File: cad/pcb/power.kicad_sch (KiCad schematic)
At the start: 32 parts, among them X1 USB_C_Plug, X2 Bat-Conn

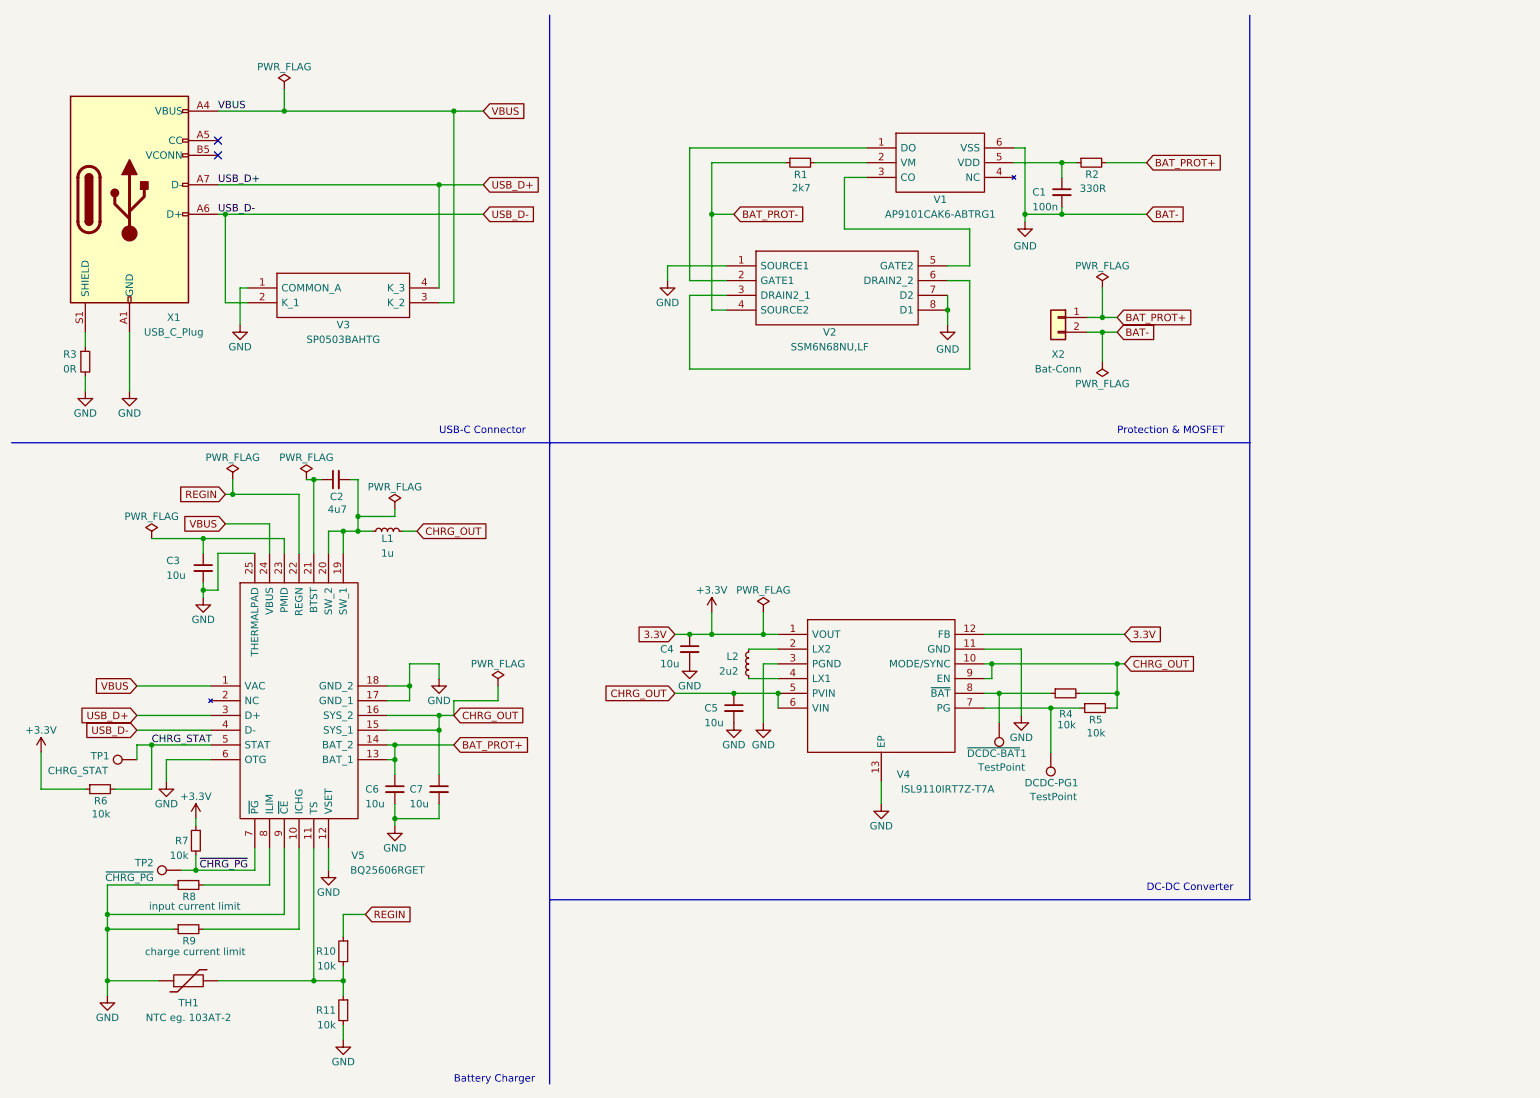
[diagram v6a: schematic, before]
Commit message: add testpoints & connectors
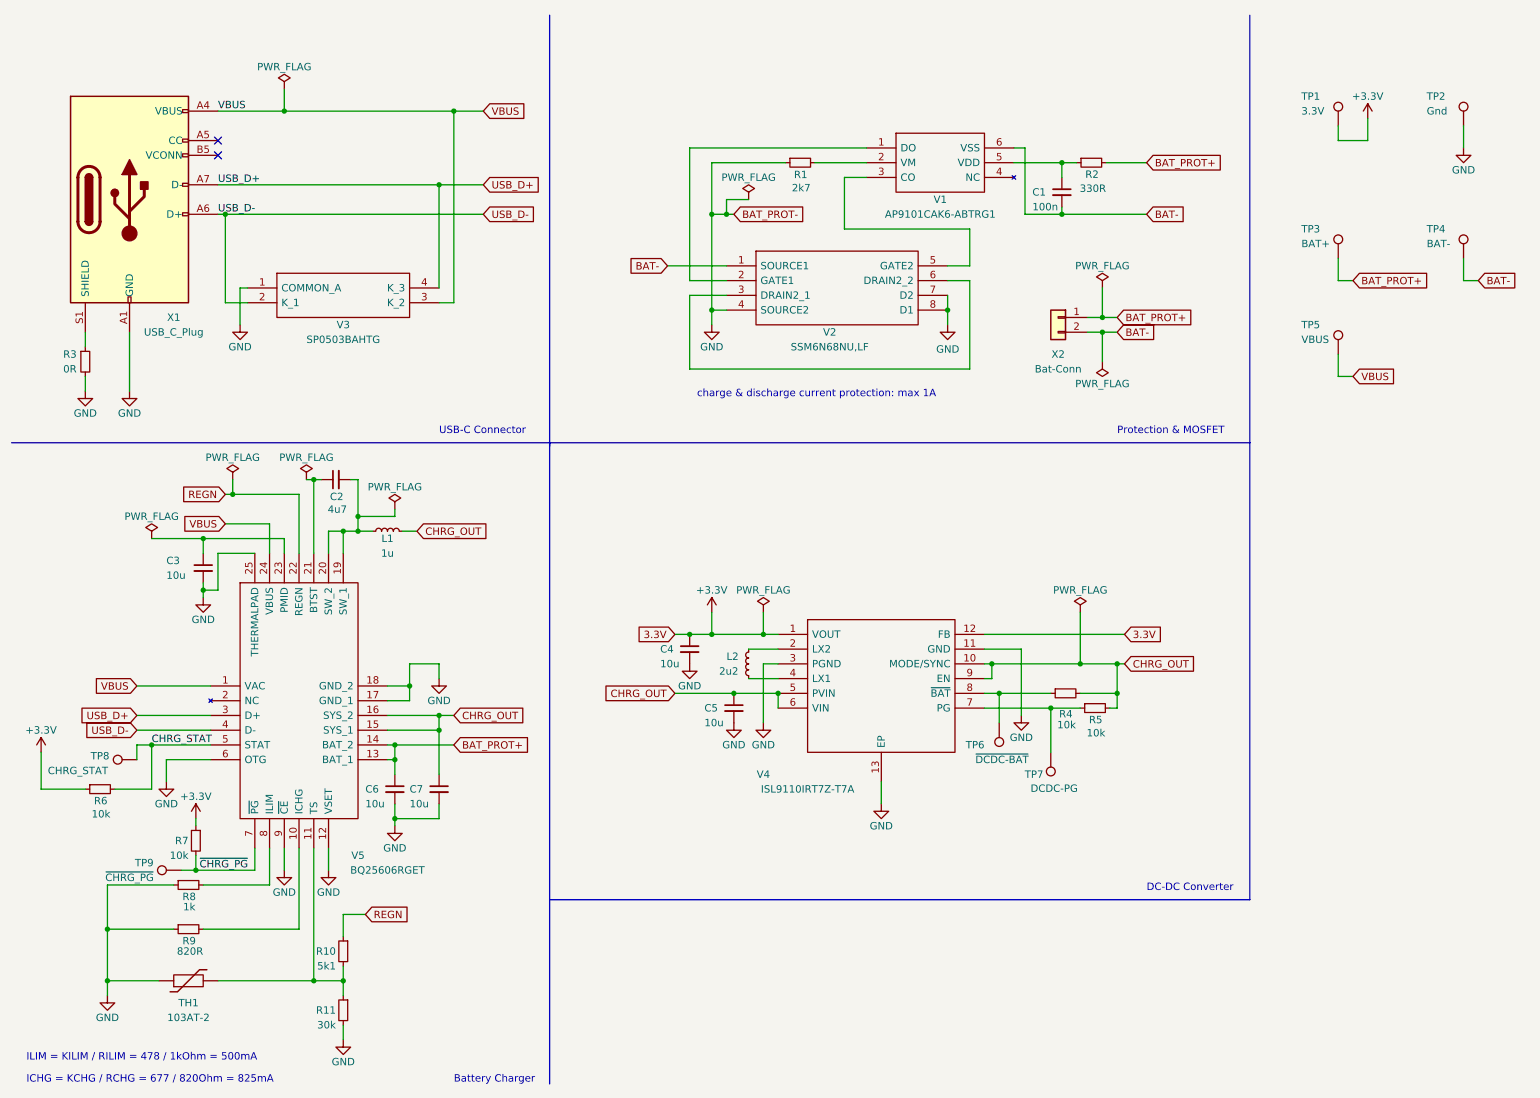
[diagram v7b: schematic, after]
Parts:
- added TP1: 3.3V, symbol Connector:TestPoint
- added TP2: Gnd, symbol Connector:TestPoint
- added TP3: BAT+, symbol Connector:TestPoint
- added TP4: BAT-, symbol Connector:TestPoint
- added TP5: VBUS, symbol Connector:TestPoint
- R10: value 10k -> 5k1
- R11: value 10k -> 30k
- R8: value input current limit -> 1k
- R9: value charge current limit -> 820R
- TH1: value NTC eg. 103AT-2 -> 103AT-2
- TP6: renamed from ~{DCDC-BAT}1; value TestPoint -> ~{DCDC-BAT}
- TP7: renamed from DCDC-PG1; value TestPoint -> DCDC-PG
- X2: footprint (none) -> Connector_JST:JST_PH_B2B-PH-SM4-TB_1x02-1MP_P2.00mm_Vertical
- renumbered TP1 to TP8, TP2 to TP9
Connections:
- net BAT_PROT- is gone; now on net GND: R1.1, V2.4 (SOURCE2)
- net +3.3V: now also TP1.1
- net BAT_PROT+: now also TP3.1
- net GND: now also TP2.1; no longer C1.2, V1.6 (VSS), V2.1 (SOURCE1), X2.2 (Pin_2)
- net VBUS: now also TP5.1
- net REGIN renamed REGN
- new net BAT-: C1.2, TP4.1, V1.6 (VSS), V2.1 (SOURCE1), X2.2 (Pin_2)
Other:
- note added: "ICHG = KCHG / RCHG = 677 / 820Ohm = 825mA"
- note added: "ILIM = KILIM / RILIM = 478 / 1kOhm = 500mA"
- note added: "charge & discharge current protection: max 1A"

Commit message: add usb-c footprint
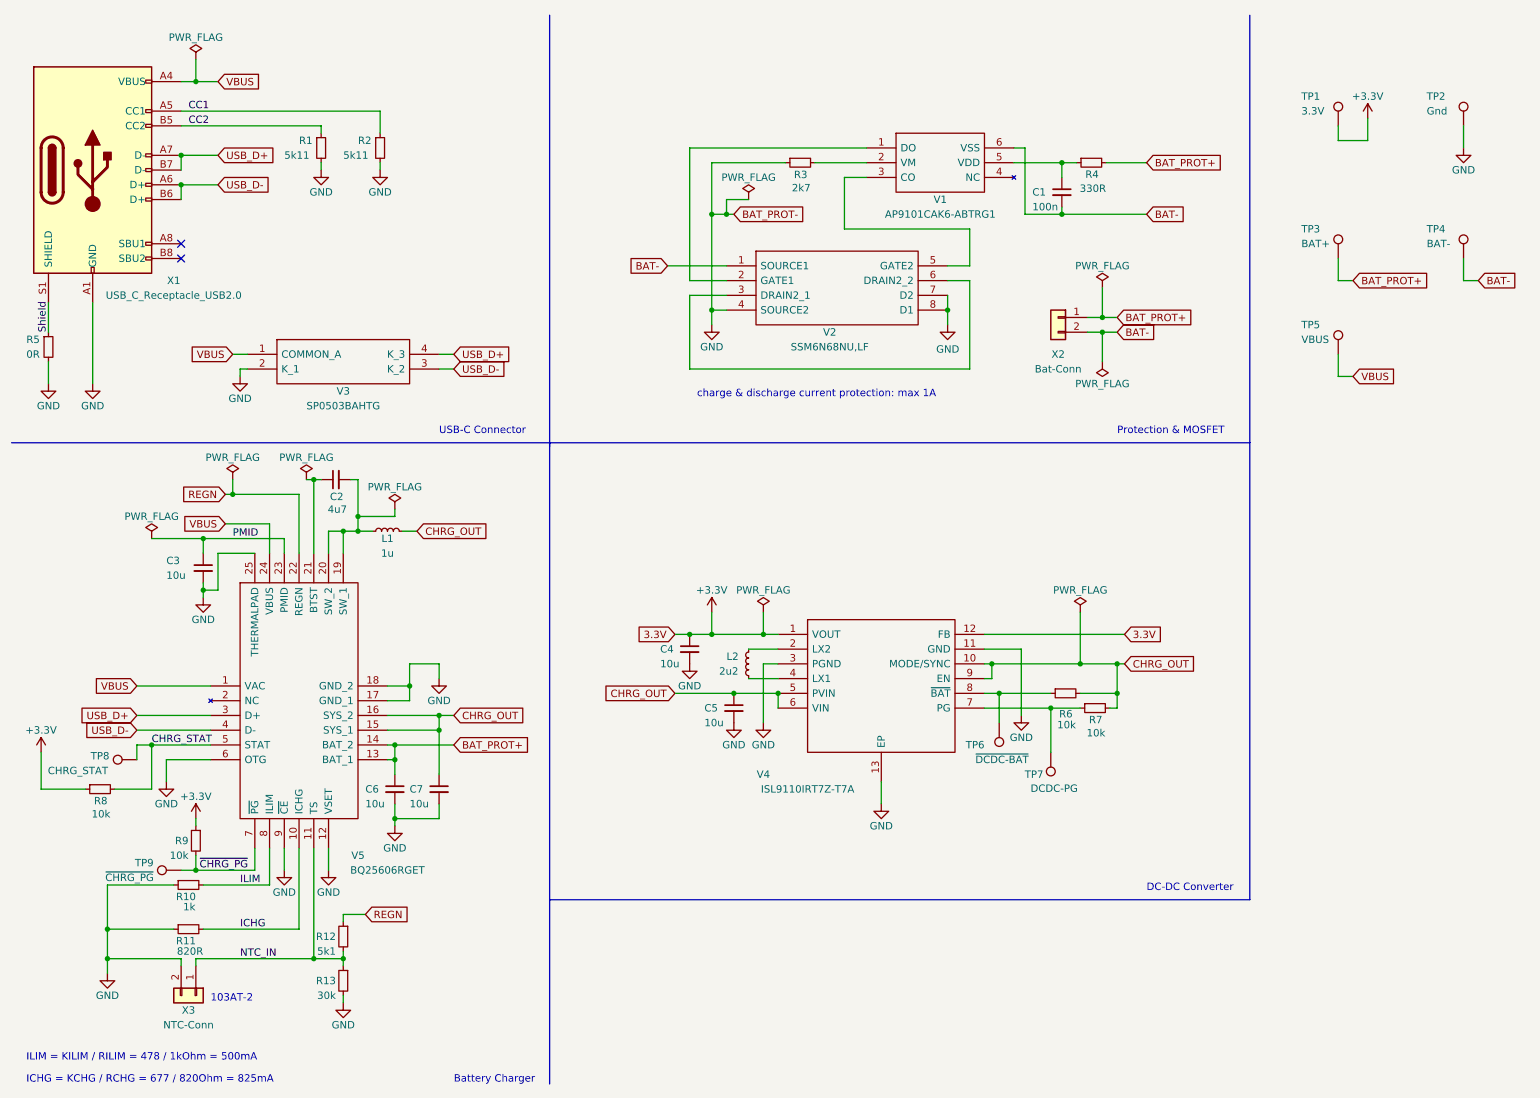
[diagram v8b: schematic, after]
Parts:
- removed TH1: 103AT-2, symbol Device:Thermistor
- removed X1: USB_C_Plug, symbol Connector:USB_C_Plug_USB2.0
- added R1, R2: 5k11, symbol Device:R_Small
- added X1: USB_C_Receptacle_USB2.0, myLib:USB_C_Receptacle_Molex_216990-0003, symbol Connector:USB_C_Receptacle_USB2.0
- added X3: NTC-Conn, Connector_JST:JST_PH_B2B-PH-SM4-TB_1x02-1MP_P2.00mm_Vertical, symbol Connector_Generic:Conn_01x02
- renumbered R8 to R10, R9 to R11, R10 to R12, R11 to R13, R1 to R3, R2 to R4, R3 to R5, R4 to R6, R5 to R7, R6 to R8, R7 to R9
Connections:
- net GND: now also V3.2 (K_1), R1.2, R2.2, X1.A1 (GND), X1.A12 (GND), X1.B1 (GND), X1.B12 (GND), X3.2 (Pin_2); no longer V3.1 (COMMON_A)
- net USB_D+: now also X1.A7 (D-), X1.B7 (D-)
- net USB_D-: now also V3.3 (K_2), X1.A6 (D+), X1.B6 (D+); no longer V3.2 (K_1)
- net VBUS: now also V3.1 (COMMON_A), X1.A4 (VBUS), X1.A9 (VBUS), X1.B4 (VBUS), X1.B9 (VBUS); no longer V3.3 (K_2)
- net NTC_IN: now reaches R12.2, R13.1, V5.11 (TS)
- net NTC_IN: now also X3.1 (Pin_1)
- net PMID: now reaches C3.1, V5.23 (PMID)
- net ICHG: now reaches R11.2, V5.10 (ICHG)
- net ILIM: now reaches R10.2, V5.8 (ILIM)
- net Shield: now reaches R5.1
- net Shield: now also X1.S1 (SHIELD)
- new net CC1: R2.1, X1.A5 (CC1)
- new net CC2: R1.1, X1.B5 (CC2)
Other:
- note added: "103AT-2"
- moved on the sheet: R12, R13, R5, V3
